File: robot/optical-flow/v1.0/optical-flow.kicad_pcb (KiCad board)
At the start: 2 copper layers, 40 x 44.5 mm, 65 parts, among them J1 Conn_ARM_JTAG_SWD_10, J2 BM09B-SRSS-TB, J3 0.1" Header, J4 SM07B-SRSS-TB, J5 SM05B-SRSS-TB, J6 SM07B-SRSS-TB, Q1 BSS138K, SW1 BTN0, SW2 SW_DIP_x04, SW3 RST, U1 STM32F407VETx, Y1 TAXM8M4RDBCCT2T, Y2 Q13FC13500005

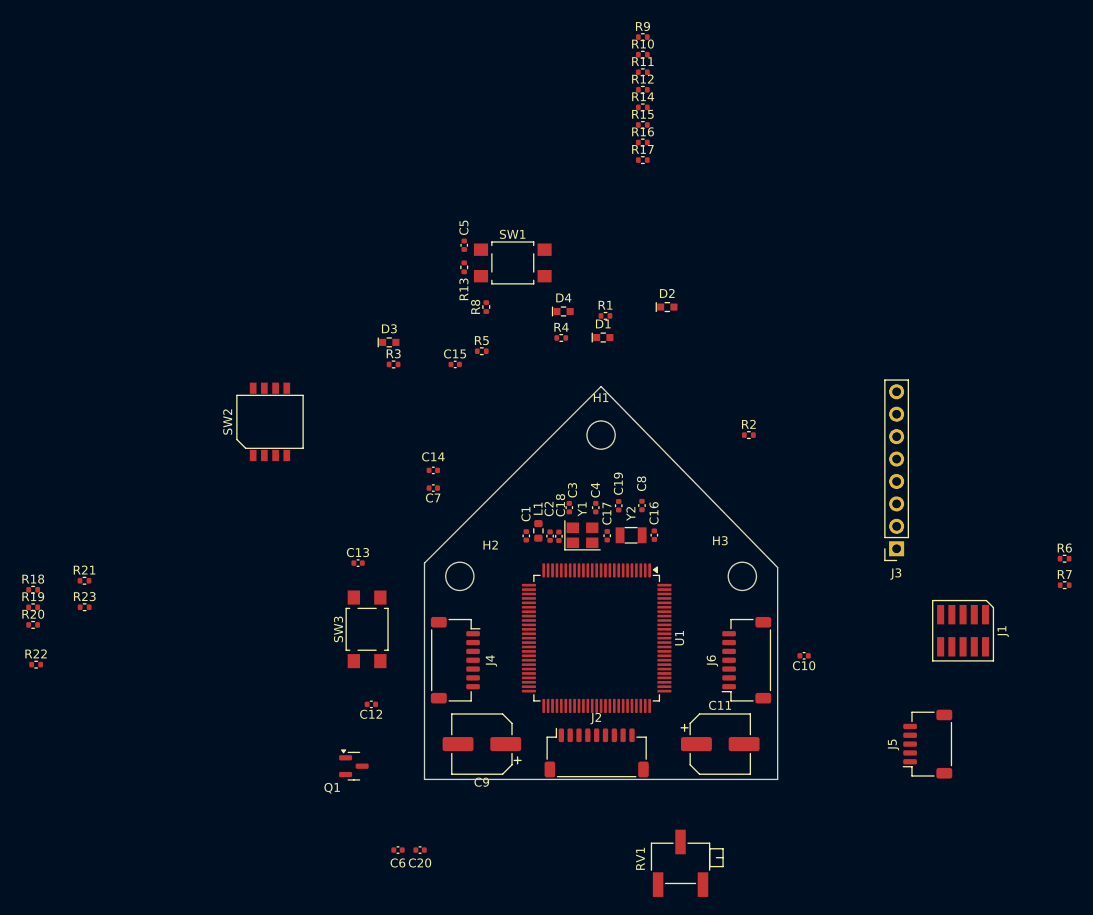
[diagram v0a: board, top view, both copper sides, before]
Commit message: Finish switch to G0 and larger space
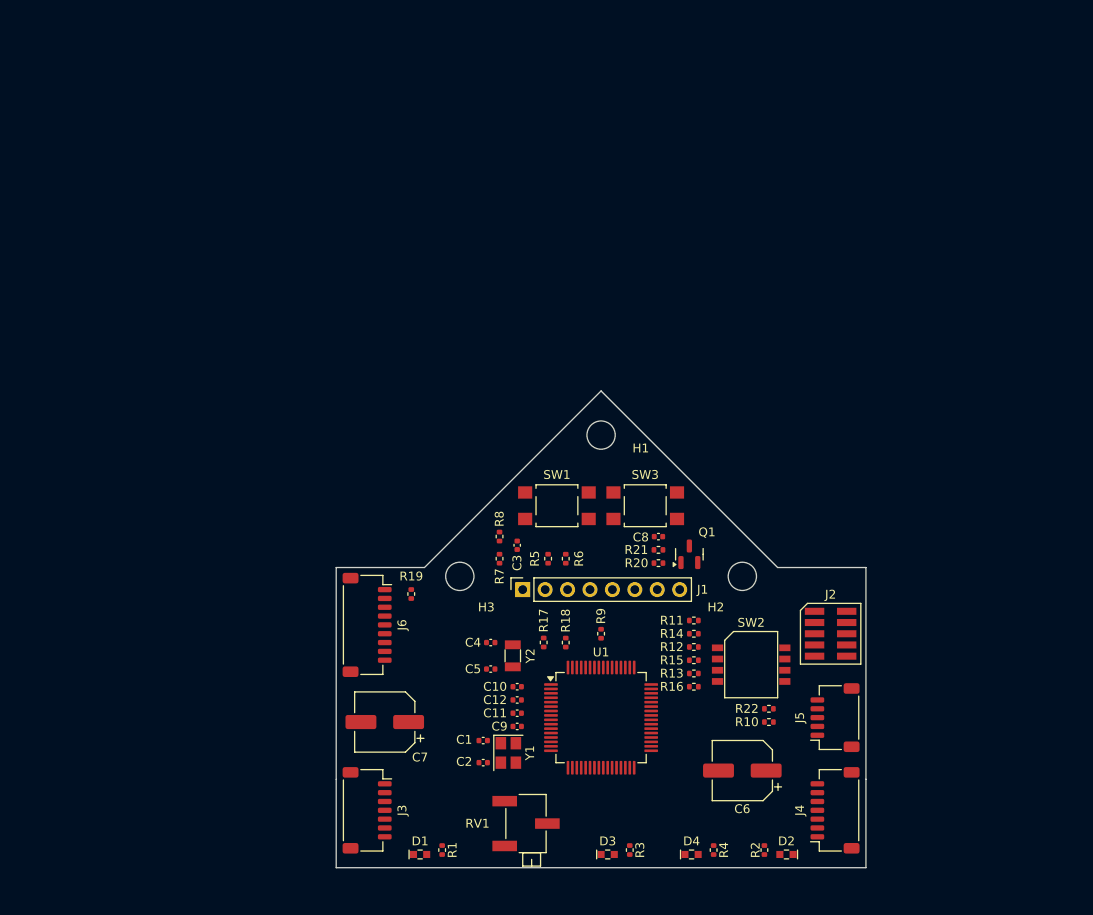
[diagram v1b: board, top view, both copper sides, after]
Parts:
- removed C13, C15, C17, C18: 100n 6.3V, Capacitor_SMD:C_0402_1005Metric
- removed C14: 100n, Capacitor_SMD:C_0402_1005Metric
- removed C16: 1u, Capacitor_SMD:C_0402_1005Metric
- removed C19, C20: 15pF 6.3V, Capacitor_SMD:C_0402_1005Metric
- removed the C3 at (162.4, 81.2)
- removed the C6 at (143.0, 120.0)
- removed the C8 at (170.6, 81.0)
- removed L1: 650 @100MHz, Resistor_SMD:R_0603_1608Metric
- removed the R2 at (182.7, 73.0)
- removed the R3 at (142.5, 65.0)
- removed the R4 at (161.5, 62.0)
- removed the R5 at (152.5, 63.5)
- removed the R7 at (218.5, 90.0)
- removed the R8 at (153.0, 58.5)
- removed the R9 at (170.7, 27.9)
- added C1: 11pF 6.3V, Capacitor_SMD:C_0402_1005Metric, F.Cu at (152.7, 107.6)
- added C2: 11pF 6.3V, Capacitor_SMD:C_0402_1005Metric, F.Cu at (152.7, 110.1)
- added C5: 15pF 6.3V, Capacitor_SMD:C_0402_1005Metric, F.Cu at (153.5, 99.5)
- added R11: 330, Resistor_SMD:R_0402_1005Metric, F.Cu at (176.5, 94.0)
- added R12: 330, Resistor_SMD:R_0402_1005Metric, F.Cu at (176.5, 97.0)
- added R13: 330, Resistor_SMD:R_0402_1005Metric, F.Cu at (176.5, 100.0)
- added R14: 10k, Resistor_SMD:R_0402_1005Metric, F.Cu at (176.5, 95.5)
- added R15: 10k, Resistor_SMD:R_0402_1005Metric, F.Cu at (176.5, 98.5)
- added R22: 330, Resistor_SMD:R_0402_1005Metric, F.Cu at (185.0, 104.0)
- C10: renamed from C7; value 4.7u 6.3V -> 1u 6.3V
- C3: renamed from C1; value 100n -> 100n 6.3V
- C4: value 11pF 6.3V -> 15pF 6.3V
- R10: value 10k -> 100k
- U1: value STM32F407VETx -> STM32G071RBTx; footprint Package_QFP:LQFP-100_14x14mm_P0.5mm -> Package_QFP:LQFP-64_10x10mm_P0.5mm
- moved R2 87.9 mm to (184.5, 120.0), turned to -90 degrees
- moved R1 81.4 mm to (148.0, 120.0), turned to -90 degrees
- moved R4 79.6 mm to (178.8, 120.0), turned to -90 degrees
- moved R10 76.9 mm to (185.0, 105.5), turned to 180 degrees
- moved R19 74.1 mm to (144.5, 91.0), turned to -90 degrees
- moved R3 72.2 mm to (169.2, 120.0), turned to -90 degrees
- moved D2 63.5 mm to (187.0, 120.5), turned to 180 degrees
- moved D4 63.2 mm to (176.2, 120.5)
- moved D3 63.1 mm to (166.8, 120.5)
- moved D1 62.1 mm to (145.5, 120.5)
- moved R16 61.9 mm to (176.5, 101.5)
- moved R17 61.6 mm to (159.5, 96.5), turned to -90 degrees
- moved SW2 61.0 mm to (183.0, 99.0), turned to -90 degrees
- moved R18 59.3 mm to (162.0, 96.5), turned to -90 degrees
- moved R5 58.6 mm to (160.0, 87.0), turned to -90 degrees
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- renumbered C10 to C11, C9 to C6, C11 to C7, C2 to C8, C5 to C9, H3 to H2, H2 to H3, J3 to J1, J1 to J2, J4 to J3, J6 to J4, J2 to J6, R17 to R1, R14 to R17, R15 to R18, R6 to R19, R18 to R2, R11 to R20, R13 to R21, R20 to R3, R22 to R4, R19 to R5, R21 to R6, R12 to R7, R1 to R8, R23 to R9
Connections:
- net /GPIO_PD11 renamed /GPIO_PB4
- C4 pad 1: Net-(U1-PH1) -> /32KHZ_CLK_REF
- J1 pad 2: /I2C_3_SCL -> /I2C_1_SCL
- J1 pad 3: /I2C_3_SDA -> /I2C_1_SDA
- J1 pad 4: /GPIO_PD9 -> /GPIO_PB6
- J1 pad 5: /GPIO_PD10 -> /GPIO_PB5
- J1 pad 7: /GPIO_PD12 -> /GPIO_PB3
- R10 pad 2: Net-(R10-Pad2) -> /MCU_BOOT_BOOT0
- R16 pad 2: /MCU_BOOT_BOOT0 -> Net-(R13-Pad1)
- R5 pad 2: /I2C_3_SCL -> /I2C_1_SCL
- R6 pad 2: /I2C_3_SDA -> /I2C_1_SDA
- SW2 pad 1: Net-(R10-Pad2) -> Net-(R11-Pad1)
- SW2 pad 3: Net-(R3-Pad1) -> Net-(R13-Pad1)
- SW2 pad 4: Net-(R2-Pad1) -> /SWCLK
- SW2 pad 5: +3.3V -> Net-(R22-Pad2)
- U1 pad 1: /LED_BLUE_2 -> /MCU_BOOT_RX
- U1 pad 10: GND -> Net-(U1-PF0)
- U1 pad 11: +3.3V -> Net-(U1-PF1)
- U1 pad 12: Net-(U1-PH0) -> /NRST
- U1 pad 13: Net-(U1-PH1) -> unconnected-(U1-PC0-Pad13)
- U1 pad 14: /NRST -> unconnected-(U1-PC1-Pad14)
- U1 pad 18: unconnected-(U1-PC3-Pad18) -> /USER_ADJ1
- U1 pad 19: +3.3V -> unconnected-(U1-PA2-Pad19)
- U1 pad 2: /LED_RED -> unconnected-(U1-PC12-Pad2)
- U1 pad 20: GND -> unconnected-(U1-PA3-Pad20)
- U1 pad 21: Net-(U1-VDDA) -> /OPTICAL_1_NSS
- U1 pad 22: Net-(U1-VDDA) -> /OPTICAL_1_SCK
- U1 pad 23: unconnected-(U1-PA0-Pad23) -> /OPTICAL_1_MISO
- U1 pad 24: /DISPLAY_~{RST} -> /OPTICAL_1_MOSI
- U1 pad 25: /DISPLAY_TX -> /OPTICAL_1_INT
- U1 pad 26: /DISPLAY_RX -> unconnected-(U1-PC5-Pad26)
- U1 pad 27: GND -> /LED_BLUE_1
- U1 pad 28: +3.3V -> /LED_GREEN
- U1 pad 29: /OPTICAL_1_NSS -> /LED_RED
- U1 pad 30: /OPTICAL_1_SCK -> /LED_BLUE_2
- U1 pad 31: /OPTICAL_1_MISO -> unconnected-(U1-PB11-Pad31)
- U1 pad 32: /OPTICAL_1_MOSI -> unconnected-(U1-PB12-Pad32)
- U1 pad 33: /OPTICAL_1_INT -> /OPTICAL_2_SCK
- U1 pad 34: unconnected-(U1-PC5-Pad34) -> /OPTICAL_2_MISO
- U1 pad 35: /USER_ADJ1 -> /OPTICAL_2_MOSI
- U1 pad 36: unconnected-(U1-PB1-Pad36) -> /OPTICAL_2_NSS
- U1 pad 37: unconnected-(U1-PB2-Pad37) -> /OPTICAL_2_INT
- U1 pad 4: unconnected-(U1-PE5-Pad4) -> /32KHZ_CLK_REF
- U1 pad 40: /DIP_0 -> unconnected-(U1-PD8-Pad40)
- U1 pad 41: /DIP_1 -> unconnected-(U1-PD9-Pad41)
- U1 pad 42: /DIP_2 -> unconnected-(U1-PA10/UCPD1_DBCC2-Pad42)
- U1 pad 43: /DIP_3 -> unconnected-(U1-PA11/PA9-Pad43)
- U1 pad 45: unconnected-(U1-PE14-Pad45) -> /SWDIO
- U1 pad 46: unconnected-(U1-PE15-Pad46) -> /SWCLK
- U1 pad 47: unconnected-(U1-PB10-Pad47) -> /DIP_0
- U1 pad 48: unconnected-(U1-PB11-Pad48) -> /DIP_1
- U1 pad 49: Net-(U1-VCAP_1) -> /DIP_2
- U1 pad 5: unconnected-(U1-PE6-Pad5) -> Net-(U1-PC15)
- U1 pad 50: +3.3V -> unconnected-(U1-PD0-Pad50)
- U1 pad 51: unconnected-(U1-PB12-Pad51) -> /USR_BTN
- U1 pad 54: unconnected-(U1-PB15-Pad54) -> /DISPLAY_~{RST}
- U1 pad 55: unconnected-(U1-PD8-Pad55) -> /DISPLAY_TX
- U1 pad 56: /GPIO_PD9 -> /DISPLAY_RX
- U1 pad 57: /GPIO_PD10 -> /GPIO_PB3
- U1 pad 59: /GPIO_PD12 -> /GPIO_PB5
- U1 pad 60: unconnected-(U1-PD13-Pad60) -> /GPIO_PB6
- U1 pad 61: unconnected-(U1-PD14-Pad61) -> /I2C_1_SDA
- U1 pad 62: /MCU_BOOT_BOOT0 -> /I2C_1_SCL
- U1 pad 64: unconnected-(U1-PC7-Pad64) -> /MCU_BOOT_TX
- U1 pad 7: unconnected-(U1-PC13-Pad7) -> +3.3V
- U1 pad 8: /32KHZ_CLK_REF -> +3.3V
- U1 pad 9: Net-(U1-PC15) -> GND
- Y1 pad 1: Net-(U1-PH0) -> Net-(U1-PF0)
- Y1 pad 3: Net-(U1-PH1) -> Net-(U1-PF1)
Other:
- board size 40 x 44.5 mm -> 60 x 54 mm
- copper layers 2 -> 4

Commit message: Optical flow routing
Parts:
- moved R10 36.9 mm to (150.0, 94.0)
- moved R22 36.0 mm to (150.0, 95.5)
- moved R9 22.0 mm to (186.5, 103.5), turned to 180 degrees
- moved R17 13.2 mm to (147.5, 102.0), turned to 0 degrees
- moved R18 12.7 mm to (150.5, 102.0), turned to 180 degrees
- moved R20 8.38 mm to (170.0, 95.5)
- moved R21 8.38 mm to (170.0, 94.0)
- moved C2 5.90 mm to (158.5, 111.0), turned to 0 degrees
- moved D4 4.00 mm to (172.2, 120.5)
- moved R4 4.00 mm to (174.8, 120.0)
- moved C6 3.20 mm to (184.0, 108.5)
- moved C8 2.50 mm to (172.5, 87.0)
- moved J2 2.32 mm to (191.5, 93.2)
- moved D3 2.00 mm to (164.8, 120.5)
- moved R3 2.00 mm to (167.2, 120.0)
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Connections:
- SW2 pad 4: /SWCLK -> Net-(R22-Pad2)
- SW2 pad 5: Net-(R22-Pad2) -> /SWCLK
- U1 pad 1: /MCU_BOOT_RX -> unconnected-(U1-PC11-Pad1)
- U1 pad 19: unconnected-(U1-PA2-Pad19) -> /MCU_BOOT_TX
- U1 pad 20: unconnected-(U1-PA3-Pad20) -> /MCU_BOOT_RX
- U1 pad 40: unconnected-(U1-PD8-Pad40) -> /DISPLAY_TX
- U1 pad 41: unconnected-(U1-PD9-Pad41) -> /DISPLAY_RX
- U1 pad 42: unconnected-(U1-PA10/UCPD1_DBCC2-Pad42) -> /DISPLAY_~{RST}
- U1 pad 51: /USR_BTN -> unconnected-(U1-PD1-Pad51)
- U1 pad 54: /DISPLAY_~{RST} -> unconnected-(U1-PD4-Pad54)
- U1 pad 55: /DISPLAY_TX -> unconnected-(U1-PD5-Pad55)
- U1 pad 56: /DISPLAY_RX -> unconnected-(U1-PD6-Pad56)
- U1 pad 64: /MCU_BOOT_TX -> /USR_BTN
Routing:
- net /NRST: track 0.00 -> 71.6 mm, vias 0 -> 3
- net GND: track 0.00 -> 68.7 mm, vias 0 -> 43
- net +5V: track 0.00 -> 54.0 mm, vias 0 -> 2
- net +3.3V: track 0.00 -> 45.3 mm, vias 0 -> 14
- net /MCU_BOOT_RX: track 0.00 -> 37.9 mm
- net /MCU_BOOT_TX: track 0.00 -> 37.7 mm
- net /SWDIO: track 0.00 -> 34.6 mm
- net Net-(R22-Pad2): track 0.00 -> 31.0 mm, vias 0 -> 2
- net /MCU_BOOT_RST: track 0.00 -> 30.1 mm, vias 0 -> 2
- net /SWCLK: track 0.00 -> 29.4 mm
- net /OPTICAL_1_INT: track 0.00 -> 28.3 mm
- net /OPTICAL_1_MOSI: track 0.00 -> 26.9 mm, vias 0 -> 2
- net /OPTICAL_1_MISO: track 0.00 -> 26.7 mm
- net /OPTICAL_2_NSS: track 0.00 -> 26.4 mm, vias 0 -> 2
- net /OPTICAL_1_SCK: track 0.00 -> 25.3 mm
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- added copper zone on In2.Cu, net +3.3V
- added copper zone on In1.Cu, net GND
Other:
- board text added: "BOOT0"
- board text added: "BTN"
- board text added: "DISP"
- board text added: "ID"
- board text added: "MCU"
- board text added: "OF1"
- board text added: "OF2"
- board text added: "OPTICAL FLOW v1.0"
- board text added: "PGM"
- board text added: "RST"
- board text added: "SSL A-Team"

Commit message: Submitted JLCPCB order
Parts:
- J2: footprint AT-Connectors:Samtec-2x5pin-0.5mm -> AT-Connectors:Samtec-2x5pin-1.27mm
- J6: value BM09B-SRSS-TB -> SM09B-SRSS-TB
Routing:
- net /USR_BTN: track 15.8 -> 16.8 mm
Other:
- board size 60 x 54 mm -> 60 x 53.7 mm
- board text added: "⌀M3"
